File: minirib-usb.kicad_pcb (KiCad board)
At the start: 2 copper layers, 60 x 30 mm, 48 parts, among them J1 USB_B_Micro, J2 Mini-DIN-6-Shielded, J3 UART, J4 UART, Q1 BS84W, Q2 BS84W, Q3 BSS138W, Q4 BS84W, Q5 BSS138W, Q6 BSS138W, Q7 BSS138W, U1 FT231XS, U2 TL071

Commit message: finalizing rev D
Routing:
- net unconnected-(J1-Pad4): track 0.00 -> 2.00 mm
- net GND: track 5.12 -> 7.02 mm
- net +5V: track 173.8 -> 175.5 mm
- net Net-(J1-Pad3): track 4.57 -> 5.30 mm
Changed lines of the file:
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@@
     (property "Sheetname" "")
     (attr exclude_from_pos_files)
-    (fp_text reference "H4" (at 0 -3.7) (layer "F.SilkS")
+    (fp_text reference "H4" (at 0 -3.7) (layer "F.SilkS") hide
       (effects (font (size 1 1) (thickness 0.15)))
     )
@@
     (property "Sheetname" "")
     (attr exclude_from_pos_files)
-    (fp_text reference "H1" (at 0 -3.7) (layer "F.SilkS")
+    (fp_text reference "H1" (at 0 -3.7) (layer "F.SilkS") hide
       (effects (font (size 1 1) (thickness 0.15)))
     )
@@
     (property "Sheetname" "")
     (attr exclude_from_pos_files)
-    (fp_text reference "H2" (at 0 -3.7) (layer "F.SilkS")
+    (fp_text reference "H2" (at 0 -3.7) (layer "F.SilkS") hide
       (effects (font (size 1 1) (thickness 0.15)))
     )
@@
     (property "Sheetname" "")
     (attr smd)
-    (fp_text reference "R1" (at 2.495 0.005 90) (layer "F.SilkS")
-      (effects (font (size 1 1) (thickness 0.15)))
+    (fp_text reference "R1" (at 2.245 0 90) (layer "F.SilkS")
+      (effects (font (size 0.75 0.75) (thickness 0.15)))
     )
     (fp_text value "22" (at 0 1.65) (layer "F.Fab")
@@
     (property "Sheetname" "")
     (attr exclude_from_pos_files)
-    (fp_text reference "H3" (at 0 -3.7) (layer "F.SilkS")
+    (fp_text reference "H3" (at 0 -3.7) (layer "F.SilkS") hide
       (effects (font (size 1 1) (thickness 0.15)))
     )
@@
     (property "Sheetname" "")
     (attr smd)
-    (fp_text reference "R2" (at -2.495 -0.005 90) (layer "F.SilkS")
-      (effects (font (size 1 1) (thickness 0.15)))
+    (fp_text reference "R2" (at -2.25 0 90) (layer "F.SilkS")
+      (effects (font (size 0.75 0.75) (thickness 0.15)))
     )
     (fp_text value "22" (at 0 1.65) (layer "F.Fab")
@@
     (property "Sheetname" "")
     (attr smd)
-    (fp_text reference "C1" (at -2.495 0 90) (layer "F.SilkS")
-      (effects (font (size 1 1) (thickness 0.15)))
+    (fp_text reference "C1" (at -2.245 0 90) (layer "F.SilkS")
+      (effects (font (size 0.75 0.75) (thickness 0.15)))
     )
     (fp_text value "4.7uF" (at 0 1.68) (layer "F.Fab")
@@
     (property "Sheetname" "")
     (attr smd)
-    (fp_text reference "C4" (at -2.495 0 90) (layer "F.SilkS")
-      (effects (font (size 1 1) (thickness 0.15)))
+    (fp_text reference "C4" (at -2.245 0 90) (layer "F.SilkS")
+      (effects (font (size 0.75 0.75) (thickness 0.15)))
     )
     (fp_text value "0.1uF" (at 0 1.68) (layer "F.Fab")
@@
       ) (layer "Eco2.User") (width 0.01) (fill solid))
   )
+  (gr_rect (start 154.75 105.45) (end 152.2 105.85) (layer "F.Mask") (width 0) (fill solid))
+  (gr_rect (start 154.75 104.8) (end 152.2 105.2) (layer "F.Mask") (width 0) (fill solid))
+  (gr_rect (start 154.75 104.15) (end 152.2 104.55) (layer "F.Mask") (width 0) (fill solid))
+  (gr_rect (start 154.75 106.1) (end 152.2 106.5) (layer "F.Mask") (width 0) (fill solid))
+  (gr_rect (start 154.75 103.5) (end 152.2 103.9) (layer "F.Mask") (width 0) (fill solid))
   (gr_arc (start 156.75 90) (mid 159.048097 90.951903) (end 160 93.25) (layer "Edge.Cuts") (width 0.05))
   (gr_arc (start 103.25 120) (mid 100.951903 119.048097) (end 100 116.75) (layer "Edge.Cuts") (width 0.05))
@@
     (effects (font (size 1 1) (thickness 0.15)) (justify mirror))
   )
+  (dimension (type aligned) (layer "Dwgs.User")
+    (pts (xy 99.75 90) (xy 99.75 120))
+    (height 14.749999)
+    (gr_text "30.0000 mm" (at 83.850001 105 90) (layer "Dwgs.User")
+      (effects (font (size 1 1) (thickness 0.15)))
+    )
+    (format (units 3) (units_format 1) (precision 4))
+    (style (thickness 0.1) (arrow_length 1.27) (text_position_mode 0) (extension_height 0.58642) (extension_offset 0.5) keep_text_aligned)
+  )
+  (dimension (type aligned) (layer "Dwgs.User")
+    (pts (xy 100 90) (xy 160 90))
+    (height -15)
+    (gr_text "60.0000 mm" (at 130 73.85) (layer "Dwgs.User")
+      (effects (font (size 1 1) (thickness 0.15)))
+    )
+    (format (units 3) (units_format 1) (precision 4))
+    (style (thickness 0.1) (arrow_length 1.27) (text_position_mode 0) (extension_height 0.58642) (extension_offset 0.5) keep_text_aligned)
+  )
   (segment (start 145.0875 104.615) (end 145.0875 103.559682) (width 0.35) (layer "F.Cu") (net 1))
   (segment (start 146.1 104.6775) (end 145.15 104.6775) (width 0.35) (layer "F.Cu") (net 1))
+  (segment (start 154.1 103.7) (end 152.2 103.7) (width 0.35) (layer "F.Cu") (net 1))
   (segment (start 145.15 104.6775) (end 145.0875 104.615) (width 0.35) (layer "F.Cu") (net 1))
   (segment (start 145.0875 103.559682) (end 144.027818 102.5) (width 0.35) (layer "F.Cu") (net 1))
@@
   (segment (start 117.75 116.5) (end 116.5 116.5) (width 0.35) (layer "F.Cu") (net 2))
   (segment (start 155.25 99.75) (end 149.25 99.75) (width 0.45) (layer "F.Cu") (net 2))
+  (segment (start 152.35 106.3) (end 154.1 106.3) (width 0.45) (layer "F.Cu") (net 2))
   (segment (start 138 105) (end 138.5 105.5) (width 0.35) (layer "F.Cu") (net 2))
   (segment (start 122.5 107.75) (end 126.25 107.75) (width 0.25) (layer "F.Cu") (net 2))
@@
   (segment (start 122.83 106.33) (end 122 105.5) (width 0.35) (layer "F.Cu") (net 15))
   (segment (start 124.1 106.33) (end 122.83 106.33) (width 0.35) (layer "F.Cu") (net 15))
-  (segment (start 151.5 108.5) (end 151 109) (width 0.35) (layer "F.Cu") (net 17))
-  (segment (start 153.1 105.65) (end 151.5 107.25) (width 0.35) (layer "F.Cu") (net 17))
-  (segment (start 151.5 107.25) (end 151.5 108.5) (width 0.35) (layer "F.Cu") (net 17))
-  (segment (start 151 109) (end 150.25 109) (width 0.35) (layer "F.Cu") (net 17))
-  (segment (start 154.1 105.65) (end 153.1 105.65) (width 0.35) (layer "F.Cu") (net 17))
-  (segment (start 152.75 105) (end 154.1 105) (width 0.35) (layer "F.Cu") (net 18))
-  (segment (start 150.255 106.75) (end 151 106.75) (width 0.35) (layer "F.Cu") (net 18))
-  (segment (start 151 106.75) (end 152.75 105) (width 0.35) (layer "F.Cu") (net 18))
+  (segment (start 154.1 104.35) (end 152.1 104.35) (width 0.35) (layer "F.Cu") (net 16))
+  (segment (start 150.25 109) (end 151.75 107.5) (width 0.35) (layer "F.Cu") (net 17))
+  (segment (start 151.75 107.5) (end 151.75 105.7) (width 0.35) (layer "F.Cu") (net 17))
+  (segment (start 151.8 105.65) (end 152.15 105.65) (width 0.35) (layer "F.Cu") (net 17))
+  (segment (start 154.1 105.65) (end 152.15 105.65) (width 0.35) (layer "F.Cu") (net 17))
+  (segment (start 152.15 105.65) (end 152.138909 105.638909) (width 0.35) (layer "F.Cu") (net 17))
+  (segment (start 151.75 105.7) (end 151.8 105.65) (width 0.35) (layer "F.Cu") (net 17))
+  (segment (start 154.1 105) (end 151.5 105) (width 0.35) (layer "F.Cu") (net 18))
+  (segment (start 151 106.75) (end 150.255 106.75) (width 0.35) (layer "F.Cu") (net 18))
+  (segment (start 151.2 105.3) (end 151.2 106.55) (width 0.35) (layer "F.Cu") (net 18))
+  (segment (start 151.2 106.55) (end 151 106.75) (width 0.35) (layer "F.Cu") (net 18))
+  (segment (start 151.5 105) (end 151.2 105.3) (width 0.35) (layer "F.Cu") (net 18))
   (segment (start 116.33 94.195) (end 116.525 94) (width 0.35) (layer "F.Cu") (net 19))
   (segment (start 116.33 96.75) (end 116.33 94.195) (width 0.35) (layer "F.Cu") (net 19))

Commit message: revision E updates
added 10k resistors to TX & DTR lines from FT231XS to allow PFETs to turn off properly when TX/DTR at 3V3. Currently they're always on (oops)
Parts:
- added R19: 10k, Resistor_SMD:R_0805_2012Metric_Pad1.20x1.40mm_HandSolder, F.Cu at (134.8, 110.5)
- added R20: 10k, Resistor_SMD:R_0805_2012Metric_Pad1.20x1.40mm_HandSolder, F.Cu at (137.2, 110.5)
- turned R9 to 90 degrees
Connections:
- Q1 pad 1: TXD -> Net-(Q1-Pad1)
- Q2 pad 1: TXD -> Net-(Q1-Pad1)
- Q4 pad 1: ~{DTR} -> Net-(Q4-Pad1)
- R3 pad 1: TXD -> Net-(Q1-Pad1)
- R9 pad 1: ~{DTR} -> Net-(Q4-Pad1)
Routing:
- net Net-(Q1-Pad1): track 0.00 -> 15.6 mm
- net TXD: track 51.2 -> 36.4 mm
- net ~{DTR}: track 23.4 -> 33.3 mm
- net Net-(Q4-Pad1): track 0.00 -> 7.38 mm
- net BUSY: track 90.1 -> 95.9 mm, vias 1 -> 3
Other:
- board text added: "MiniRIB USB Rev E"
- board text removed: "MiniRIB USB Rev D"

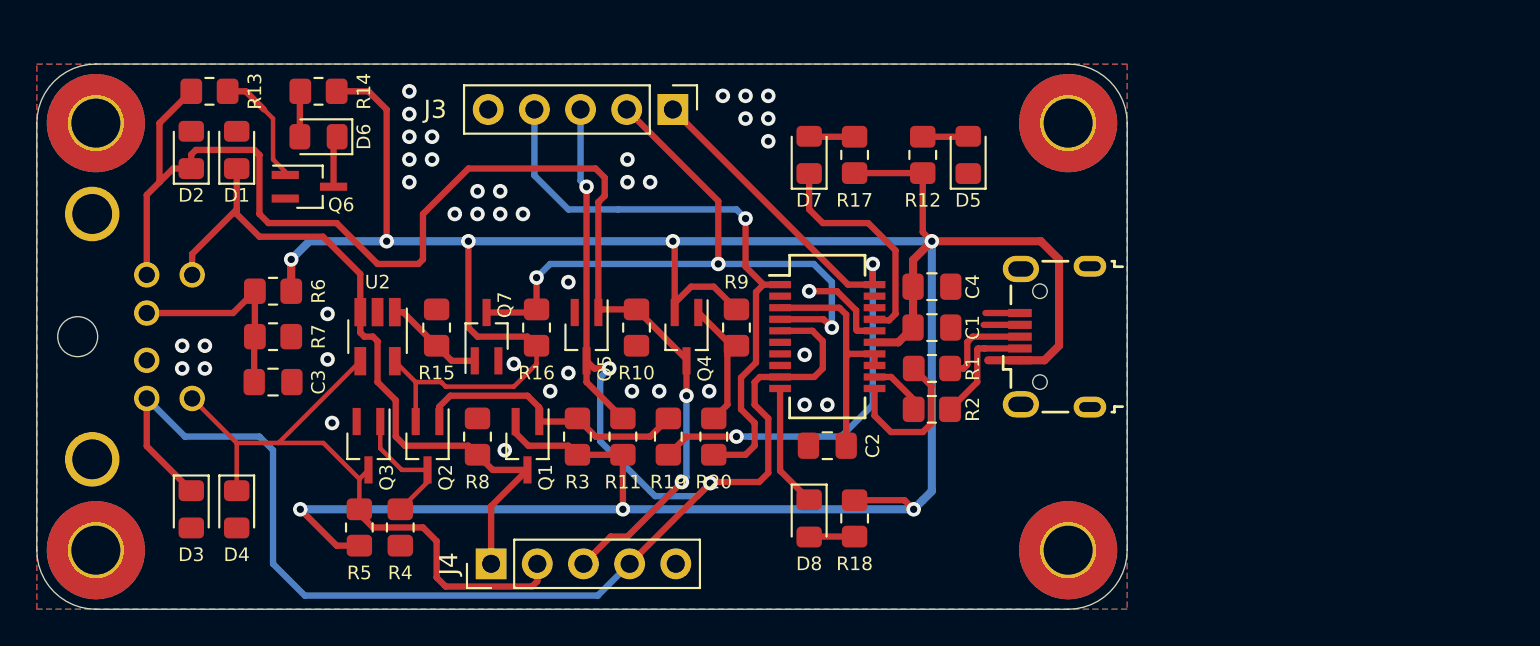
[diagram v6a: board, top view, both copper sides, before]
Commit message: PCB assembly updates
updates to revision E to add LCSC components to allow for JLCPCB manufacture
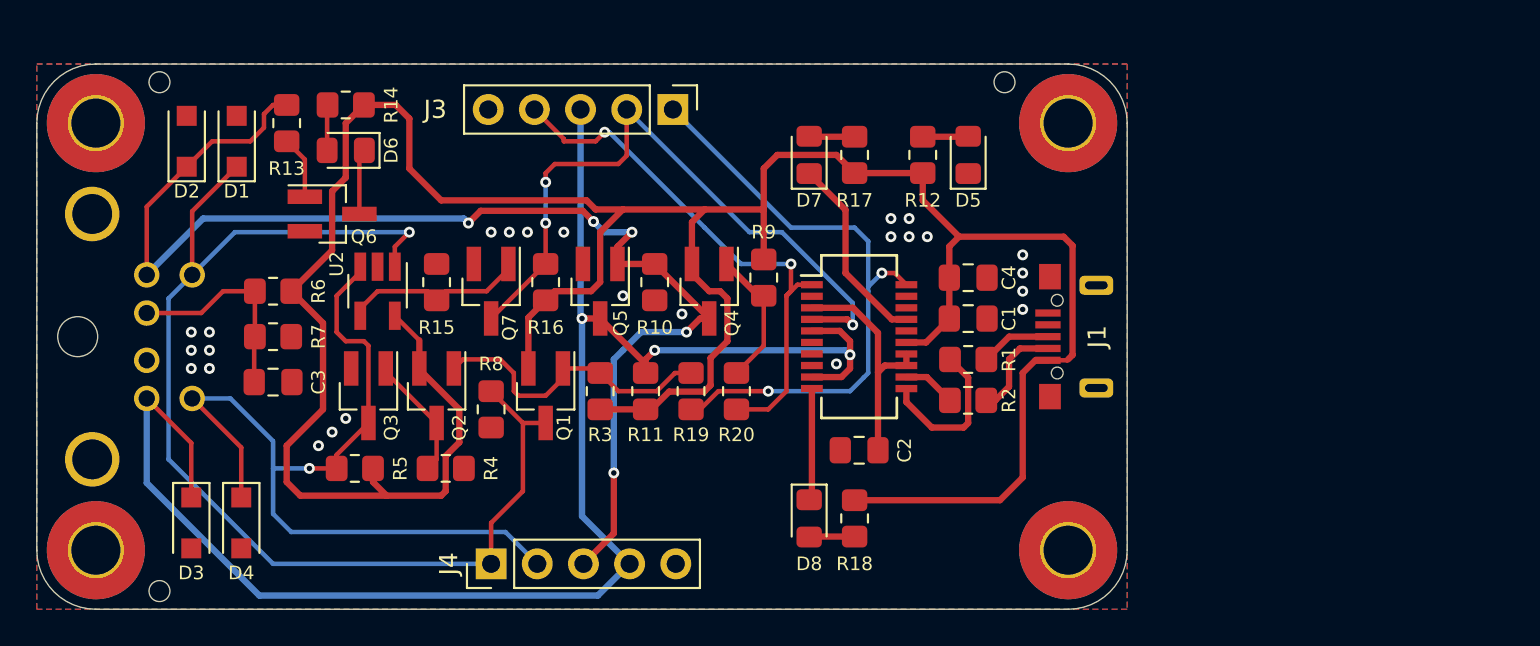
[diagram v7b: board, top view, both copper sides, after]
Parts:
- added th1: tooling-hole, lcsc-comps:tooling-hole, F.Cu at (106.8, 91.0)
- added th2: tooling-hole, lcsc-comps:tooling-hole, F.Cu at (153.2, 91.0)
- added th3: tooling-hole, lcsc-comps:tooling-hole, F.Cu at (106.8, 119.0)
- C3: value 220pF -> 0.1uF
- D1, D2, D3, D4: footprint Diode_SMD:D_0805_2012Metric_Pad1.15x1.40mm_HandSolder -> Diode_SMD:D_SOD-123F
- J1: value USB_B_Micro -> U254-051N-4BH83-F1B; footprint Connector_USB:USB_Micro-B_Wuerth_629105150521 -> lcsc-comps:U254-051N-4BH83-F1B
- Q1, Q2, Q4: value BS84W -> LBSS84LT1G; footprint Package_TO_SOT_SMD:SOT-323_SC-70_Handsoldering -> Package_TO_SOT_SMD:SOT-23_Handsoldering
- Q3, Q5, Q6, Q7: value BSS138W -> 2N7002; footprint Package_TO_SOT_SMD:SOT-323_SC-70_Handsoldering -> Package_TO_SOT_SMD:SOT-23_Handsoldering
- U2: value TL071 -> LMV321
- moved R13 4.60 mm to (113.8, 93.2), turned to -90 degrees
- moved R4 4.10 mm to (122.5, 112.2), turned to 180 degrees
- moved J1 3.75 mm to (159.8, 105.0)
- moved R5 3.26 mm to (117.5, 112.2), turned to 180 degrees
- moved R9 3.13 mm to (140.0, 101.8)
- moved Q1 2.93 mm to (128.0, 108.2)
- moved Q4 2.80 mm to (137.0, 102.5)
- moved R11 2.80 mm to (133.5, 108.0)
- moved R19 2.80 mm to (136.0, 108.0)
- moved R20 2.80 mm to (138.5, 108.0)
- moved R3 2.80 mm to (131.0, 108.0)
- moved Q2 2.80 mm to (122.0, 108.2)
- moved Q3 2.75 mm to (118.2, 108.2)
- moved R10 2.69 mm to (134.0, 102.0)
- moved Q5 2.61 mm to (131.0, 102.5)
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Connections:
- U2 pad 1: Net-(Q7-Pad1) -> BUS-
- U2 pad 3: BUS- -> BUS+
- U2 pad 4: BUS+ -> Net-(Q7-Pad1)
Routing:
- net BUS-: track 39.3 -> 65.1 mm, vias 0 -> 1
- net +5V: track 175.8 -> 160.2 mm, vias 8 -> 0
- net BUS+: track 36.3 -> 48.8 mm, vias 0 -> 1
- net GND: track 7.02 -> 0.00 mm, vias 41 -> 25
- net BUSY: track 95.9 -> 90.6 mm
- net Net-(Q7-Pad1): track 5.51 -> 10.2 mm
- net ~{BUSY}: track 72.9 -> 69.6 mm, vias 2 -> 5
- net ~{DTR}: track 33.3 -> 30.1 mm, vias 1 -> 2
- net Net-(Q6-Pad1): track 6.50 -> 3.46 mm
- net TXD: track 36.4 -> 34.3 mm
- net unconnected-(J1-Pad4): track 2.00 -> 0.00 mm
- net ~{TXLED}: track 12.5 -> 10.7 mm
- net Net-(J1-Pad3): track 5.30 -> 3.91 mm
- net Net-(Q1-Pad1): track 15.6 -> 16.5 mm
- net Net-(J1-Pad2): track 6.31 -> 5.46 mm
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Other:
- board text added: "BUS+"
- board text added: "BUS-"
- board text added: "BUSY"
- board text added: "GND"
- board text added: "RS232"
- board text added: "RXD"
- board text added: "SB9600"
- board text added: "TXD"
- board text added: "~{BUSY}"
- board text added: "~{CTS}"
- board text added: "~{DTR}"
